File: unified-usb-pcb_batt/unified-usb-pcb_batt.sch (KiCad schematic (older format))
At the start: 34 parts, among them J1 QI, J2 USB_C_Receptacle_USB2.0, J3 USB_Out, J4 BATT, J5 THERM, U1 SRV05-4, U2 DW01A, U3 TP4056, U4 FS8205

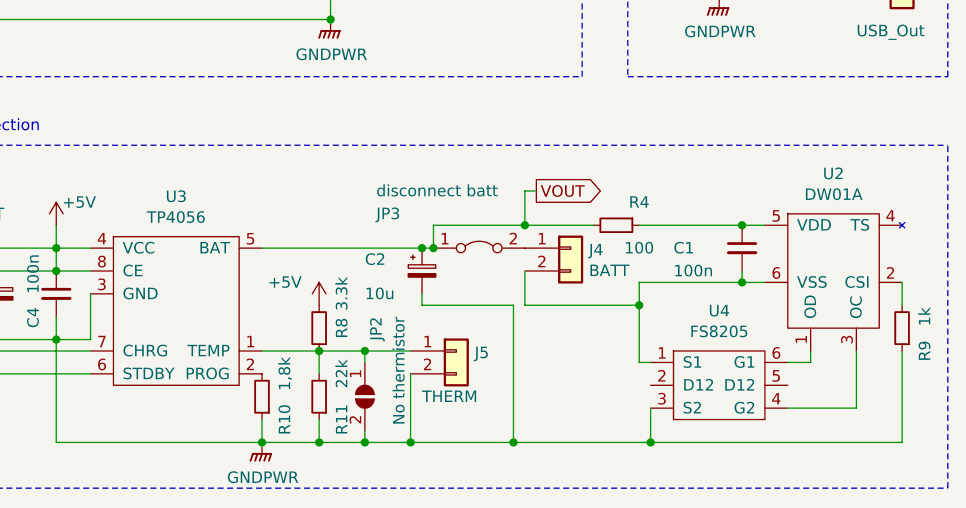
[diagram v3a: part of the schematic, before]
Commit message: replaced jumper with smd switch
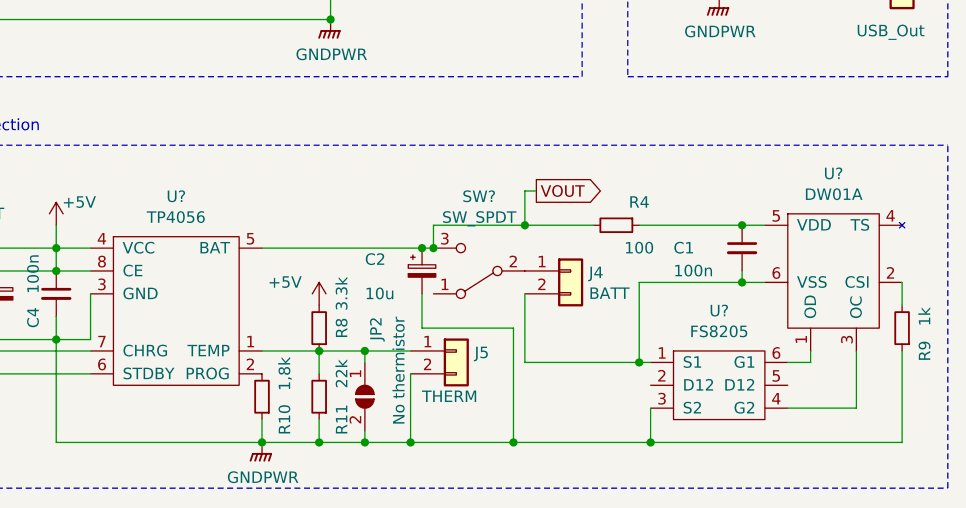
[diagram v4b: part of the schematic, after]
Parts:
- removed JP3: disconnect batt, Connector_PinHeader_2.54mm:PinHeader_1x02_P2.54mm_Vertical, symbol Jumper:Jumper_2_Bridged
- removed U2: DW01A, Package_TO_SOT_SMD:SOT-23-6, symbol TP4056:DW01A
- removed U3: TP4056, Package_SO:SOP-8-1EP_4.57x4.57mm_P1.27mm_EP4.57x4.45mm, symbol TP4056:TP4056
- removed U4: FS8205, Package_TO_SOT_SMD:SOT-23-6, symbol TP4056:FS8205
- added SW?: SW_SPDT, kicad-keyboard-parts:ESP3020, symbol Switch:SW_SPDT
- added U?: TP4056, Package_SO:SOP-8-1EP_4.57x4.57mm_P1.27mm_EP4.57x4.45mm, symbol kicad-keyboard-parts:TP4056
- added U?: DW01A, Package_TO_SOT_SMD:SOT-23-6, symbol kicad-keyboard-parts:DW01A
- added U?: FS8205, Package_TO_SOT_SMD:SOT-23-6, symbol kicad-keyboard-parts:FS8205
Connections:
- net +5V: now also U?.4 (VCC), U?.8 (CE)
- net GNDPWR: now also U?.3 (GND), U?.3 (S2)
- net VOUT: now also SW?.3 (C), U?.5 (BAT)
- net chgsense: now also U?.7 (CHRG)
- net at J4.1 (Pin_1): now also SW?.2 (B)
- net at C1.2, J4.2 (Pin_2): now also U?.1 (S1), U?.6 (VSS)
- net at J5.1 (Pin_1), JP2.1 (A), R11.2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: now also U?.1 (TEMP)
- net at R10.2: now also U?.2 (PROG)
- net at R5.1: now also U?.6 (STDBY)
- net at R9.2: now also U?.2 (CSI)
- net at C1.1, R4.1: now also U?.5 (VDD)
- new net: U?.1 (OD), U?.6 (G1)
- new net: U?.3 (OC), U?.4 (G2)
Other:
- moved on the sheet: J4
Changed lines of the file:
@@
 L Connector_Generic:Conn_01x02 J4
 U 1 1 5E8AB5AC
-P 3900 3600
-F 0 "J4" H 3980 3592 50  0000 L CNN
-F 1 "BATT" H 3980 3501 50  0000 L CNN
-F 2 "Connector_JST:JST_SH_SM02B-SRSS-TB_1x02-1MP_P1.00mm_Horizontal" H 3900 3600 50  0001 C CNN
-F 3 "~" H 3900 3600 50  0001 C CNN
-	1    3900 3600
+P 3900 3700
+F 0 "J4" H 3980 3692 50  0000 L CNN
+F 1 "BATT" H 3980 3601 50  0000 L CNN
+F 2 "Connector_JST:JST_SH_SM02B-SRSS-TB_1x02-1MP_P1.00mm_Horizontal" H 3900 3700 50  0001 C CNN
+F 3 "~" H 3900 3700 50  0001 C CNN
+	1    3900 3700
 	1    0    0    -1
 $EndComp
@@
 Wire Wire Line
 	5150 1100 5300 1100
-$Comp
-L TP4056:TP4056 U3
-U 1 1 5E8BD80B
-P 2200 3850
-F 0 "U3" H 2175 4325 50  0000 C CNN
-F 1 "TP4056" H 2175 4234 50  0000 C CNN
-F 2 "Package_SO:SOP-8-1EP_4.57x4.57mm_P1.27mm_EP4.57x4.45mm" H 2150 4350 50  0001 C CNN
-F 3 "https://datasheet.lcsc.com/szlcsc/1906261508_Nanjing-Extension-Microelectronics-TP4056-42-ESOP8_C16581.pdf" H 2150 4350 50  0001 C CNN
-	1    2200 3850
-	1    0    0    -1
-$EndComp
-$Comp
-L TP4056:DW01A U2
-U 1 1 5E8C090A
-P 5050 3700
-F 0 "U2" H 5050 4125 50  0000 C CNN
-F 1 "DW01A" H 5050 4034 50  0000 C CNN
-F 2 "Package_TO_SOT_SMD:SOT-23-6" H 4850 4050 50  0001 C CNN
-F 3 "https://datasheet.lcsc.com/szlcsc/Fortune-Semicon-DW01A-G_C61503.pdf" H 4850 4050 50  0001 C CNN
-	1    5050 3700
-	1    0    0    -1
-$EndComp
-$Comp
-L TP4056:FS8205 U4
-U 1 1 5E8C23B9
-P 4550 4200
-F 0 "U4" H 4550 4525 50  0000 C CNN
-F 1 "FS8205" H 4550 4434 50  0000 C CNN
-F 2 "Package_TO_SOT_SMD:SOT-23-6" H 4500 4450 50  0001 C CNN
-F 3 "https://datasheet.lcsc.com/szlcsc/Fortune-Semicon-FS8205_C32254.pdf" H 4500 4450 50  0001 C CNN
-	1    4550 4200
-	1    0    0    -1
-$EndComp
 $Comp
 L Device:Polyfuse_Small F2
@@
 	3200 4450 3000 4450
 Connection ~ 3000 4450
-Wire Wire Line
-	3700 3700 3700 3850
-Wire Wire Line
-	3700 3850 4200 3850
-Wire Wire Line
-	4200 3850 4200 4100
 $Comp
 L Device:CP_Small C3
@@
 Wire Wire Line
 	4650 3750 4200 3750
-Wire Wire Line
-	4200 3750 4200 3850
 Connection ~ 4650 3750
-Connection ~ 4200 3850
 $Comp
 L Device:C_Small C4
@@
 	1800 3800 1800 4000
 Wire Wire Line
-	3200 4450 3650 4450
-$Comp
-L Jumper:Jumper_2_Bridged JP3
-U 1 1 5E8F2064
-P 3500 3600
-F 0 "JP3" H 3050 3750 50  0000 L CNN
-F 1 "disconnect batt" H 3050 3850 50  0000 L CNN
-F 2 "Connector_PinHeader_2.54mm:PinHeader_1x02_P2.54mm_Vertical" H 3500 3600 50  0001 C CNN
-F 3 "~" H 3500 3600 50  0001 C CNN
-	1    3500 3600
-	1    0    0    -1
-$EndComp
-Wire Wire Line
-	3250 3800 3250 3850
-Wire Wire Line
-	3250 3850 3650 3850
-Wire Wire Line
-	3650 3850 3650 4450
-Connection ~ 3650 4450
-Wire Wire Line
-	3650 4450 4250 4450
-Wire Wire Line
 	3700 3500 3300 3500
 Wire Wire Line
@@
 Wire Wire Line
 	3300 3600 3250 3600
-Connection ~ 3300 3600
 Wire Wire Line
 	3250 3600 2550 3600
@@
 	3400 2300 3400 1850
 Connection ~ 2350 1900
+$Comp
+L kicad-keyboard-parts:TP4056 U?
+U 1 1 5E8F2E62
+P 2200 3850
+F 0 "U?" H 2175 4325 50  0000 C CNN
+F 1 "TP4056" H 2175 4234 50  0000 C CNN
+F 2 "Package_SO:SOP-8-1EP_4.57x4.57mm_P1.27mm_EP4.57x4.45mm" H 2150 4350 50  0001 C CNN
+F 3 "https://datasheet.lcsc.com/szlcsc/1906261508_Nanjing-Extension-Microelectronics-TP4056-42-ESOP8_C16581.pdf" H 2150 4350 50  0001 C CNN
+	1    2200 3850
+	1    0    0    -1
+$EndComp
+$Comp
+L kicad-keyboard-parts:DW01A U?
+U 1 1 5E8F46BF
+P 5050 3700
+F 0 "U?" H 5050 4125 50  0000 C CNN
+F 1 "DW01A" H 5050 4034 50  0000 C CNN
+F 2 "Package_TO_SOT_SMD:SOT-23-6" H 4850 4050 50  0001 C CNN
+F 3 "https://datasheet.lcsc.com/szlcsc/Fortune-Semicon-DW01A-G_C61503.pdf" H 4850 4050 50  0001 C CNN
+	1    5050 3700
+	1    0    0    -1
+$EndComp
+$Comp
+L kicad-keyboard-parts:FS8205 U?
+U 1 1 5E8F556E
+P 4550 4200
+F 0 "U?" H 4550 4525 50  0000 C CNN
+F 1 "FS8205" H 4550 4434 50  0000 C CNN
+F 2 "Package_TO_SOT_SMD:SOT-23-6" H 4500 4450 50  0001 C CNN
+F 3 "https://datasheet.lcsc.com/szlcsc/Fortune-Semicon-FS8205_C32254.pdf" H 4500 4450 50  0001 C CNN
+	1    4550 4200
+	1    0    0    -1
+$EndComp
+$Comp
+L Switch:SW_SPDT SW?
+U 1 1 5E8F7463
+P 3500 3700
+F 0 "SW?" H 3500 3375 50  0000 C CNN
+F 1 "SW_SPDT" H 3500 3466 50  0000 C CNN
+F 2 "kicad-keyboard-parts:ESP3020" H 3500 3700 50  0001 C CNN
+F 3 "https://www.ece.com.tw/images/cgcustom/file020190722095856.pdf" H 3500 3700 50  0001 C CNN
+	1    3500 3700
+	-1   0    0    1
+$EndComp
+Connection ~ 3300 3600
+Wire Wire Line
+	4200 3750 4200 4100
+Wire Wire Line
+	3700 3800 3700 4100
+Wire Wire Line
+	3700 4100 4200 4100
+Connection ~ 4200 4100
+Wire Wire Line
+	3200 4450 3650 4450
+Wire Wire Line
+	3250 3950 3650 3950
+Wire Wire Line
+	3650 3950 3650 4450
+Wire Wire Line
+	3250 3800 3250 3950
+Connection ~ 3650 4450
+Wire Wire Line
+	3650 4450 4250 4450
 $EndSCHEMATC

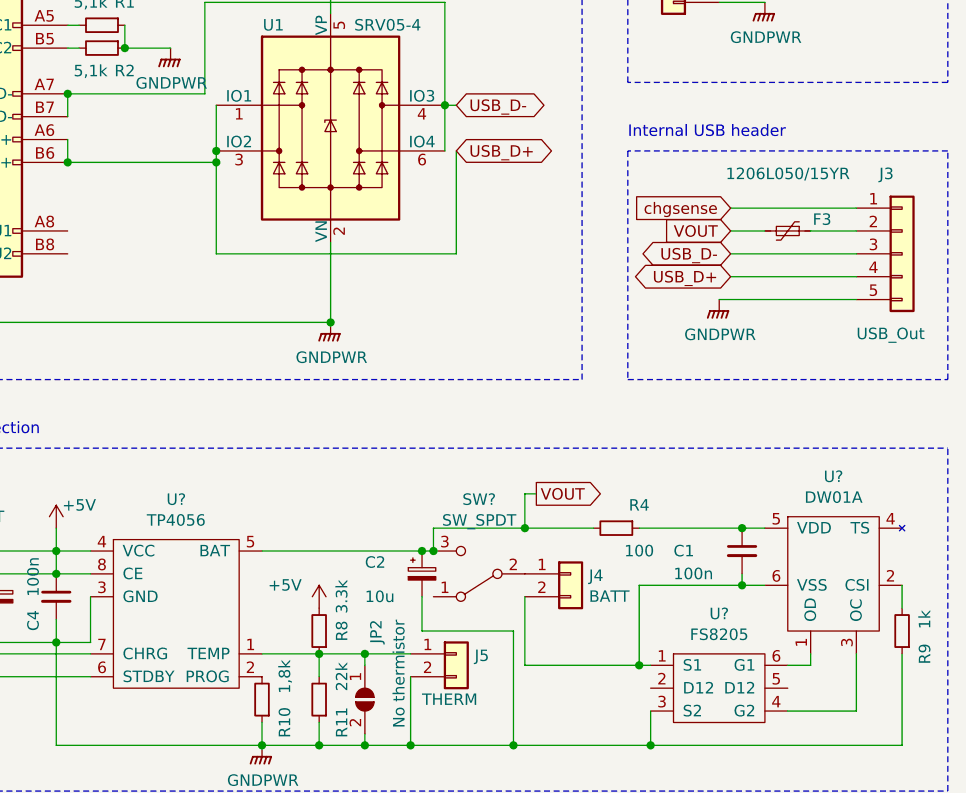
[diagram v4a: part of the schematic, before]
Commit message: added 3d models, changed tp4056 footprint
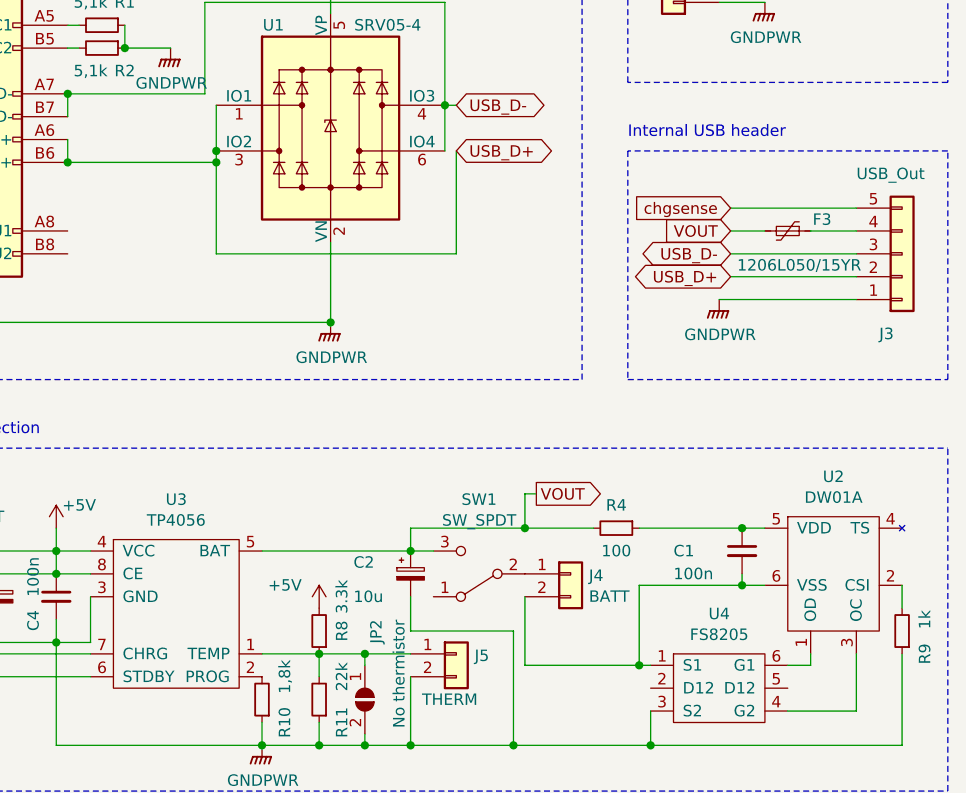
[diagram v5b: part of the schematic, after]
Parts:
- U3: renamed from U?; footprint Package_SO:SOP-8-1EP_4.57x4.57mm_P1.27mm_EP4.57x4.45mm -> Package_SO:SOIC-8-1EP_3.9x4.9mm_P1.27mm_EP2.29x3mm
- gave numbers to parts that had none: 3
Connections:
- net GNDPWR: now also J3.1 (Pin_1); no longer J3.5 (Pin_5)
- net USB_D+: now also J3.2 (Pin_2); no longer J3.4 (Pin_4)
- net chgsense: now also J3.5 (Pin_5); no longer J3.1 (Pin_1)
- net at F3.1: now also J3.4 (Pin_4); no longer J3.2 (Pin_2)
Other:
- moved on the sheet: C2
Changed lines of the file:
@@
 F 3 "~" H 5350 2300 50  0001 C CNN
 	1    5350 2300
-	1    0    0    -1
+	1    0    0    1
 $EndComp
 Text GLabel 3400 1650 2    50   BiDi ~ 0
@@
 U 1 1 5E9933A3
 P 4100 3500
-F 0 "R4" V 4000 3600 50  0000 C CNN
-F 1 "100" V 4200 3600 50  0000 C CNN
+F 0 "R4" V 4000 3500 50  0000 C CNN
+F 1 "100" V 4200 3500 50  0000 C CNN
 F 2 "Resistor_SMD:R_0603_1608Metric" H 4100 3500 50  0001 C CNN
 F 3 "~" H 4100 3500 50  0001 C CNN
@@
 L Device:CP_Small C2
 U 1 1 5E9A1A52
-P 3250 3700
-F 0 "C2" H 3000 3750 50  0000 L CNN
-F 1 "10u" H 3000 3600 50  0000 L CNN
-F 2 "Capacitor_Tantalum_SMD:CP_EIA-3216-18_Kemet-A" H 3250 3700 50  0001 C CNN
-F 3 "~" H 3250 3700 50  0001 C CNN
-	1    3250 3700
+P 3200 3700
+F 0 "C2" H 2950 3750 50  0000 L CNN
+F 1 "10u" H 2950 3600 50  0000 L CNN
+F 2 "Capacitor_Tantalum_SMD:CP_EIA-3216-18_Kemet-A" H 3200 3700 50  0001 C CNN
+F 3 "~" H 3200 3700 50  0001 C CNN
+	1    3200 3700
 	1    0    0    -1
 $EndComp
@@
 P 4850 2200
 F 0 "F3" V 4800 2350 50  0000 C CNN
-F 1 "1206L050/15YR" V 4600 2200 50  0000 C CNN
+F 1 "1206L050/15YR" V 5000 2250 50  0000 C CNN
 F 2 "Fuse:Fuse_1206_3216Metric" H 4900 2000 50  0001 L CNN
 F 3 "https://datasheet.lcsc.com/szlcsc/1810252220_Fuzetec-Tech-FSMD050-1206-R_C220147.pdf" H 4850 2200 50  0001 C CNN
@@
 Wire Wire Line
 	1800 3800 1800 4000
-Wire Wire Line
-	3700 3500 3300 3500
-Wire Wire Line
-	3300 3500 3300 3600
 Connection ~ 3700 3500
-Wire Wire Line
-	3300 3600 3250 3600
-Wire Wire Line
-	3250 3600 2550 3600
-Connection ~ 3250 3600
 Wire Wire Line
 	3000 4400 3000 4450
@@
 Connection ~ 2350 1900
 $Comp
-L kicad-keyboard-parts:TP4056 U?
+L kicad-keyboard-parts:TP4056 U3
 U 1 1 5E8F2E62
 P 2200 3850
-F 0 "U?" H 2175 4325 50  0000 C CNN
+F 0 "U3" H 2175 4325 50  0000 C CNN
 F 1 "TP4056" H 2175 4234 50  0000 C CNN
-F 2 "Package_SO:SOP-8-1EP_4.57x4.57mm_P1.27mm_EP4.57x4.45mm" H 2150 4350 50  0001 C CNN
+F 2 "Package_SO:SOIC-8-1EP_3.9x4.9mm_P1.27mm_EP2.29x3mm" H 2150 4350 50  0001 C CNN
 F 3 "https://datasheet.lcsc.com/szlcsc/1906261508_Nanjing-Extension-Microelectronics-TP4056-42-ESOP8_C16581.pdf" H 2150 4350 50  0001 C CNN
 	1    2200 3850
@@
 $EndComp
 $Comp
-L kicad-keyboard-parts:DW01A U?
+L kicad-keyboard-parts:DW01A U2
 U 1 1 5E8F46BF
 P 5050 3700
-F 0 "U?" H 5050 4125 50  0000 C CNN
+F 0 "U2" H 5050 4125 50  0000 C CNN
 F 1 "DW01A" H 5050 4034 50  0000 C CNN
 F 2 "Package_TO_SOT_SMD:SOT-23-6" H 4850 4050 50  0001 C CNN
@@
 $EndComp
 $Comp
-L kicad-keyboard-parts:FS8205 U?
+L kicad-keyboard-parts:FS8205 U4
 U 1 1 5E8F556E
 P 4550 4200
-F 0 "U?" H 4550 4525 50  0000 C CNN
+F 0 "U4" H 4550 4525 50  0000 C CNN
 F 1 "FS8205" H 4550 4434 50  0000 C CNN
 F 2 "Package_TO_SOT_SMD:SOT-23-6" H 4500 4450 50  0001 C CNN
@@
 $EndComp
 $Comp
-L Switch:SW_SPDT SW?
+L Switch:SW_SPDT SW1
 U 1 1 5E8F7463
 P 3500 3700
-F 0 "SW?" H 3500 3375 50  0000 C CNN
+F 0 "SW1" H 3500 3375 50  0000 C CNN
 F 1 "SW_SPDT" H 3500 3466 50  0000 C CNN
 F 2 "kicad-keyboard-parts:ESP3020" H 3500 3700 50  0001 C CNN
@@
 	-1   0    0    1
 $EndComp
-Connection ~ 3300 3600
 Wire Wire Line
 	4200 3750 4200 4100
@@
 	3200 4450 3650 4450
 Wire Wire Line
-	3250 3950 3650 3950
-Wire Wire Line
 	3650 3950 3650 4450
-Wire Wire Line
-	3250 3800 3250 3950
 Connection ~ 3650 4450
 Wire Wire Line
 	3650 4450 4250 4450
+Connection ~ 3200 3600
+Wire Wire Line
+	3200 3600 2550 3600
+Wire Wire Line
+	3200 3950 3200 3800
+Wire Wire Line
+	3200 3600 3300 3600
+Wire Wire Line
+	3200 3950 3650 3950
+Wire Wire Line
+	3200 3500 3200 3600
+Wire Wire Line
+	3200 3500 3700 3500
 $EndSCHEMATC

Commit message: started working on pcb layout
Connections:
- net at J4.1 (Pin_1): now also C1.2, U2.6 (VSS), U4.1 (S1); no longer SW1.2 (B)
- new net: J4.2 (Pin_2), SW1.2 (B)
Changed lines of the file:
@@
 L Connector_Generic:Conn_01x02 J4
 U 1 1 5E8AB5AC
-P 3900 3700
-F 0 "J4" H 3980 3692 50  0000 L CNN
-F 1 "BATT" H 3980 3601 50  0000 L CNN
-F 2 "Connector_JST:JST_SH_SM02B-SRSS-TB_1x02-1MP_P1.00mm_Horizontal" H 3900 3700 50  0001 C CNN
-F 3 "~" H 3900 3700 50  0001 C CNN
-	1    3900 3700
-	1    0    0    -1
+P 3900 3800
+F 0 "J4" H 3980 3792 50  0000 L CNN
+F 1 "BATT" H 3980 3701 50  0000 L CNN
+F 2 "Connector_JST:JST_SH_SM02B-SRSS-TB_1x02-1MP_P1.00mm_Horizontal" H 3900 3800 50  0001 C CNN
+F 3 "~" H 3900 3800 50  0001 C CNN
+	1    3900 3800
+	1    0    0    1
 $EndComp
 $Comp

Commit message: finished pcb
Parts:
- added H1, H2, H3, H4: MountingHole_Pad, MountingHole:MountingHole_2.7mm_M2.5_DIN965_Pad, symbol Mechanical:MountingHole_Pad
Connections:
- net GNDPWR: now also H1.1, H2.1, H3.1, H4.1
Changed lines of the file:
@@
 Wire Wire Line
 	3200 3500 3700 3500
+$Comp
+L Mechanical:MountingHole_Pad H1
+U 1 1 5E8DE6EE
+P 5850 900
+F 0 "H1" H 5950 949 50  0000 L CNN
+F 1 "MountingHole_Pad" H 5950 858 50  0000 L CNN
+F 2 "MountingHole:MountingHole_2.7mm_M2.5_DIN965_Pad" H 5850 900 50  0001 C CNN
+F 3 "~" H 5850 900 50  0001 C CNN
+	1    5850 900
+	1    0    0    -1
+$EndComp
+$Comp
+L Mechanical:MountingHole_Pad H2
+U 1 1 5E8DF691
+P 5850 1200
+F 0 "H2" H 5950 1249 50  0000 L CNN
+F 1 "MountingHole_Pad" H 5950 1158 50  0000 L CNN
+F 2 "MountingHole:MountingHole_2.7mm_M2.5_DIN965_Pad" H 5850 1200 50  0001 C CNN
+F 3 "~" H 5850 1200 50  0001 C CNN
+	1    5850 1200
+	1    0    0    -1
+$EndComp
+$Comp
+L Mechanical:MountingHole_Pad H3
+U 1 1 5E8DFD93
+P 5850 1500
+F 0 "H3" H 5950 1549 50  0000 L CNN
+F 1 "MountingHole_Pad" H 5950 1458 50  0000 L CNN
+F 2 "MountingHole:MountingHole_2.7mm_M2.5_DIN965_Pad" H 5850 1500 50  0001 C CNN
+F 3 "~" H 5850 1500 50  0001 C CNN
+	1    5850 1500
+	1    0    0    -1
+$EndComp
+$Comp
+L Mechanical:MountingHole_Pad H4
+U 1 1 5E8E0080
+P 5850 1800
+F 0 "H4" H 5950 1849 50  0000 L CNN
+F 1 "MountingHole_Pad" H 5950 1758 50  0000 L CNN
+F 2 "MountingHole:MountingHole_2.7mm_M2.5_DIN965_Pad" H 5850 1800 50  0001 C CNN
+F 3 "~" H 5850 1800 50  0001 C CNN
+	1    5850 1800
+	1    0    0    -1
+$EndComp
+Wire Wire Line
+	5850 1000 5750 1000
+Wire Wire Line
+	5750 1000 5750 1300
+Wire Wire Line
+	5750 1300 5850 1300
+Wire Wire Line
+	5750 1300 5750 1600
+Wire Wire Line
+	5750 1600 5850 1600
+Connection ~ 5750 1300
+Wire Wire Line
+	5750 1600 5750 1900
+Wire Wire Line
+	5750 1900 5850 1900
+Connection ~ 5750 1600
+$Comp
+L power:GNDPWR #PWR0101
+U 1 1 5E8EB80F
+P 5850 1900
+F 0 "#PWR0101" H 5850 1700 50  0001 C CNN
+F 1 "GNDPWR" H 5854 1746 50  0000 C CNN
+F 2 "" H 5850 1850 50  0001 C CNN
+F 3 "" H 5850 1850 50  0001 C CNN
+	1    5850 1900
+	1    0    0    -1
+$EndComp
+Connection ~ 5850 1900
 $EndSCHEMATC

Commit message: cosmetic changes
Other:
- note added: "Mounting Holes"
- moved on the sheet: H1, H2, H3, H4
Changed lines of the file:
@@
 L Mechanical:MountingHole_Pad H1
 U 1 1 5E8DE6EE
-P 5850 900
-F 0 "H1" H 5950 949 50  0000 L CNN
-F 1 "MountingHole_Pad" H 5950 858 50  0000 L CNN
-F 2 "MountingHole:MountingHole_2.7mm_M2.5_DIN965_Pad" H 5850 900 50  0001 C CNN
-F 3 "~" H 5850 900 50  0001 C CNN
-	1    5850 900
+P 6000 1250
+F 0 "H1" H 6100 1299 50  0000 L CNN
+F 1 "MountingHole_Pad" H 6100 1208 50  0000 L CNN
+F 2 "MountingHole:MountingHole_2.7mm_M2.5_DIN965_Pad" H 6000 1250 50  0001 C CNN
+F 3 "~" H 6000 1250 50  0001 C CNN
+	1    6000 1250
 	1    0    0    -1
 $EndComp
@@
 L Mechanical:MountingHole_Pad H2
 U 1 1 5E8DF691
-P 5850 1200
-F 0 "H2" H 5950 1249 50  0000 L CNN
-F 1 "MountingHole_Pad" H 5950 1158 50  0000 L CNN
-F 2 "MountingHole:MountingHole_2.7mm_M2.5_DIN965_Pad" H 5850 1200 50  0001 C CNN
-F 3 "~" H 5850 1200 50  0001 C CNN
-	1    5850 1200
+P 6000 1550
+F 0 "H2" H 6100 1599 50  0000 L CNN
+F 1 "MountingHole_Pad" H 6100 1508 50  0000 L CNN
+F 2 "MountingHole:MountingHole_2.7mm_M2.5_DIN965_Pad" H 6000 1550 50  0001 C CNN
+F 3 "~" H 6000 1550 50  0001 C CNN
+	1    6000 1550
 	1    0    0    -1
 $EndComp
@@
 L Mechanical:MountingHole_Pad H3
 U 1 1 5E8DFD93
-P 5850 1500
-F 0 "H3" H 5950 1549 50  0000 L CNN
-F 1 "MountingHole_Pad" H 5950 1458 50  0000 L CNN
-F 2 "MountingHole:MountingHole_2.7mm_M2.5_DIN965_Pad" H 5850 1500 50  0001 C CNN
-F 3 "~" H 5850 1500 50  0001 C CNN
-	1    5850 1500
+P 6000 1850
+F 0 "H3" H 6100 1899 50  0000 L CNN
+F 1 "MountingHole_Pad" H 6100 1808 50  0000 L CNN
+F 2 "MountingHole:MountingHole_2.7mm_M2.5_DIN965_Pad" H 6000 1850 50  0001 C CNN
+F 3 "~" H 6000 1850 50  0001 C CNN
+	1    6000 1850
 	1    0    0    -1
 $EndComp
@@
 L Mechanical:MountingHole_Pad H4
 U 1 1 5E8E0080
-P 5850 1800
-F 0 "H4" H 5950 1849 50  0000 L CNN
-F 1 "MountingHole_Pad" H 5950 1758 50  0000 L CNN
-F 2 "MountingHole:MountingHole_2.7mm_M2.5_DIN965_Pad" H 5850 1800 50  0001 C CNN
-F 3 "~" H 5850 1800 50  0001 C CNN
-	1    5850 1800
+P 6000 2150
+F 0 "H4" H 6100 2199 50  0000 L CNN
+F 1 "MountingHole_Pad" H 6100 2108 50  0000 L CNN
+F 2 "MountingHole:MountingHole_2.7mm_M2.5_DIN965_Pad" H 6000 2150 50  0001 C CNN
+F 3 "~" H 6000 2150 50  0001 C CNN
+	1    6000 2150
 	1    0    0    -1
 $EndComp
 Wire Wire Line
-	5850 1000 5750 1000
+	6000 1350 5900 1350
 Wire Wire Line
-	5750 1000 5750 1300
+	5900 1350 5900 1650
 Wire Wire Line
-	5750 1300 5850 1300
+	5900 1650 6000 1650
 Wire Wire Line
-	5750 1300 5750 1600
+	5900 1650 5900 1950
 Wire Wire Line
-	5750 1600 5850 1600
-Connection ~ 5750 1300
+	5900 1950 6000 1950
+Connection ~ 5900 1650
 Wire Wire Line
-	5750 1600 5750 1900
+	5900 1950 5900 2250
 Wire Wire Line
-	5750 1900 5850 1900
-Connection ~ 5750 1600
+	5900 2250 6000 2250
+Connection ~ 5900 1950
 $Comp
 L power:GNDPWR #PWR0101
 U 1 1 5E8EB80F
-P 5850 1900
-F 0 "#PWR0101" H 5850 1700 50  0001 C CNN
-F 1 "GNDPWR" H 5854 1746 50  0000 C CNN
-F 2 "" H 5850 1850 50  0001 C CNN
-F 3 "" H 5850 1850 50  0001 C CNN
-	1    5850 1900
+P 6000 2250
+F 0 "#PWR0101" H 6000 2050 50  0001 C CNN
+F 1 "GNDPWR" H 6004 2096 50  0000 C CNN
+F 2 "" H 6000 2200 50  0001 C CNN
+F 3 "" H 6000 2200 50  0001 C CNN
+	1    6000 2250
 	1    0    0    -1
 $EndComp
-Connection ~ 5850 1900
+Connection ~ 6000 2250
+Wire Notes Line style solid
+	5750 700  5750 2850
+Wire Notes Line style solid
+	5750 2850 7000 2850
+Wire Notes Line style solid
+	7000 2850 7000 700
+Wire Notes Line style solid
+	7000 700  5750 700
+Text Notes 5750 650  0    50   ~ 0
+Mounting Holes
 $EndSCHEMATC
